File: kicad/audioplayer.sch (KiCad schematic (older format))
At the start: 29 parts, among them J1 Panel, J2 Charge_USB, J3 Speakers, J4 RFID, SW1 POWER, U1 PB-500, U2 ESP32-nodeMCU, U3 OLED, U4 GY-521, U5 VS1053/SD_breakout, U6 ULN2003, U7 HW-323

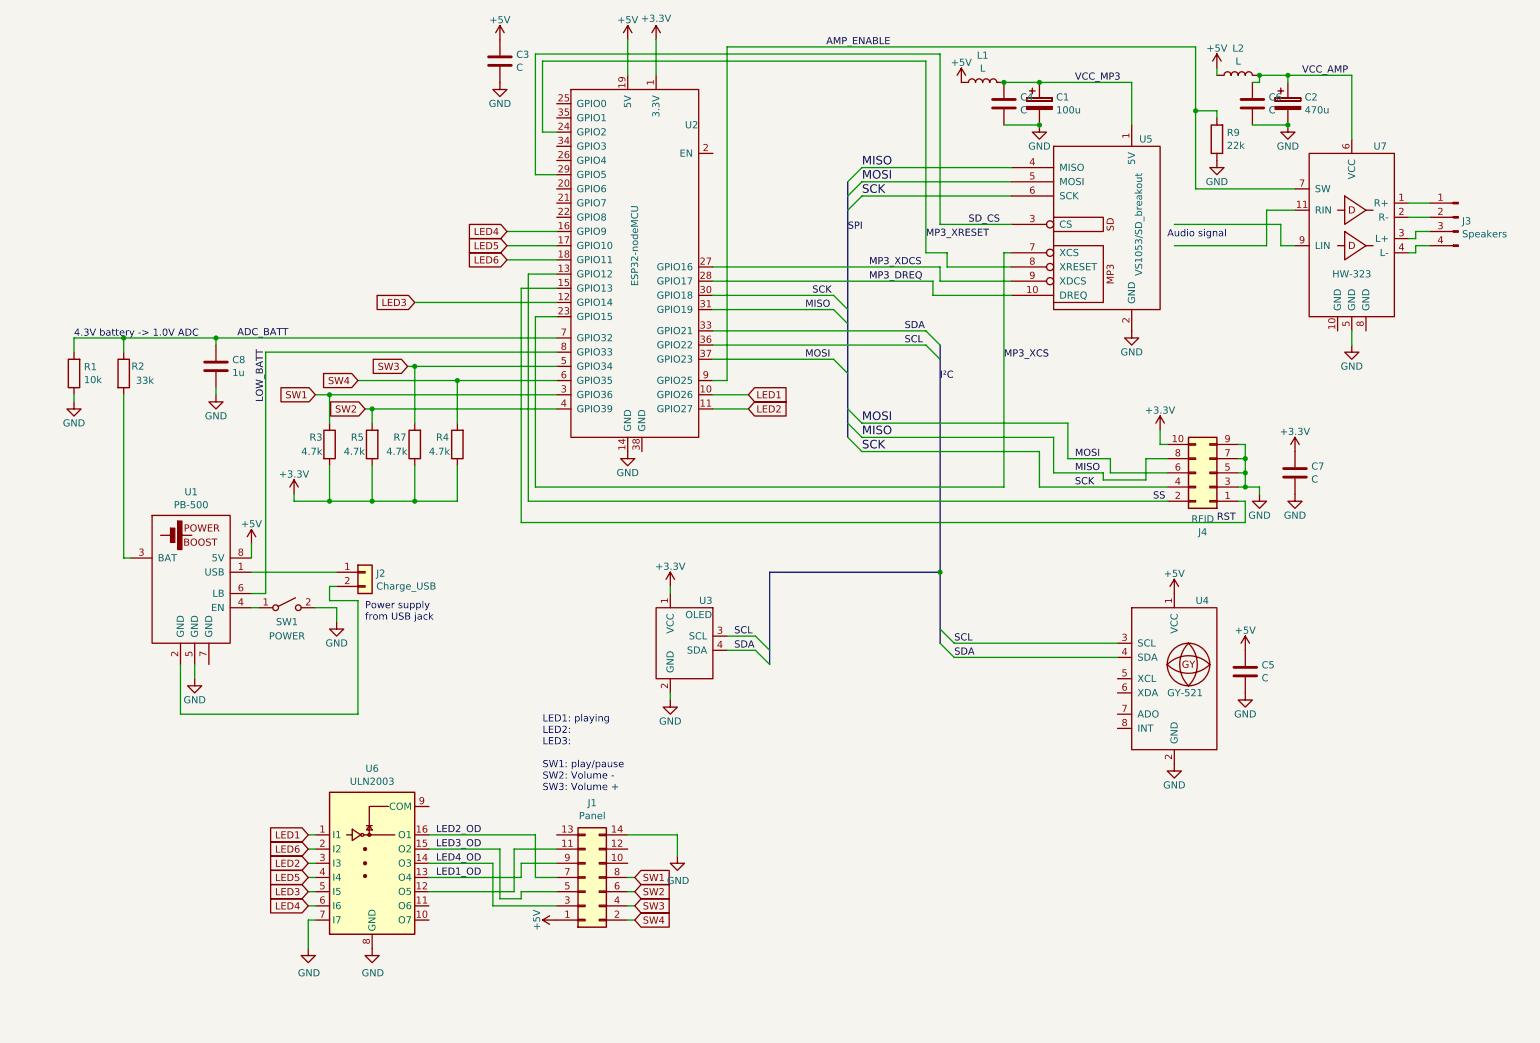
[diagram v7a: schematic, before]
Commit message: board revision 03
better ground handling, vastly reduced background noise
added reconstruction filter to vs1053 output
added possibillity to add headphone jack
use smd darlington array
add diode for battery low signal
add diode for charging connector (reverse polarity protection just in case)
use 10-pin panel connector and swapped connections for better PCB routing
swapped some GPIO-Pins for better PCB routing (i.e. RFID SS,SCK)
use restor ladder for button GPIOs
removed supply decoupling for SD/MP3 board
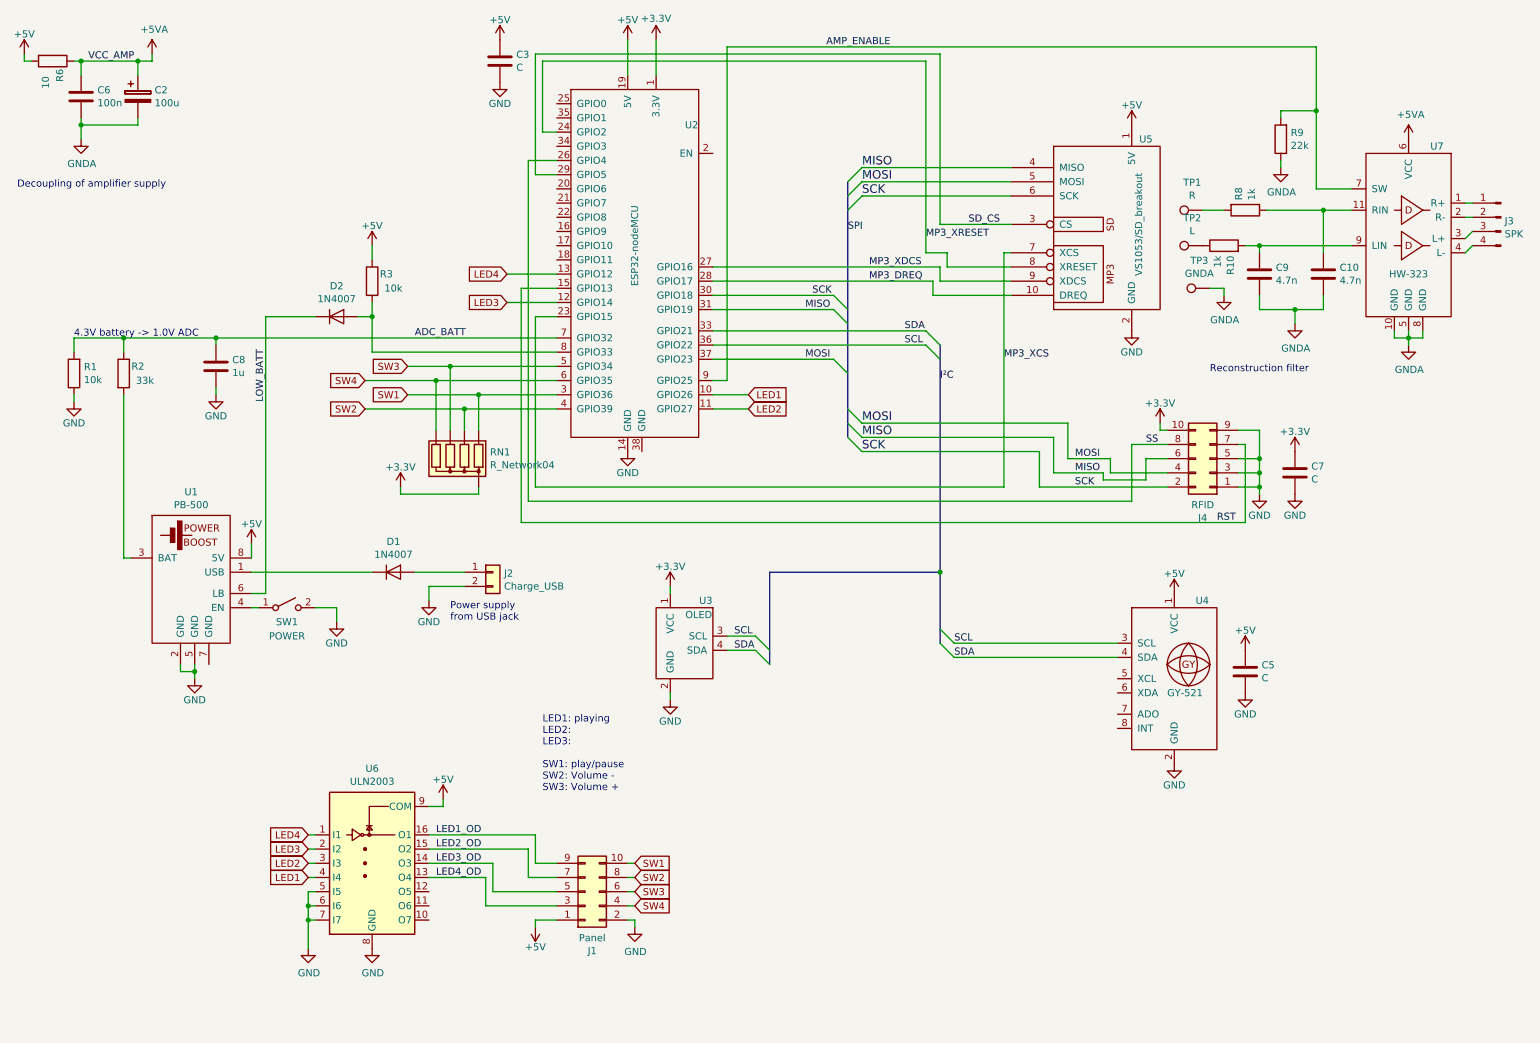
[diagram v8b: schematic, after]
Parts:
- removed C1: 100u, Capacitor_THT:CP_Radial_D10.0mm_P5.00mm, symbol Device:CP
- removed C4: C, Capacitor_THT:C_Disc_D5.1mm_W3.2mm_P5.00mm, symbol Device:C
- removed J1: Panel, Connector_PinHeader_2.54mm:PinHeader_2x07_P2.54mm_Vertical, symbol Connector_Generic:Conn_02x07_Odd_Even
- removed L1, L2: L, Inductor_THT:L_Axial_L6.6mm_D2.7mm_P10.16mm_Horizontal_Vishay_IM-2, symbol Device:L
- removed R4, R5, R7: 4.7k, Resistor_THT:R_Axial_DIN0204_L3.6mm_D1.6mm_P7.62mm_Horizontal, symbol Device:R
- added C10, C9: 4.7n, Capacitor_THT:C_Rect_L7.0mm_W2.5mm_P5.00mm, symbol Device:C
- added D1, D2: 1N4007, Diode_THT:D_DO-41_SOD81_P10.16mm_Horizontal, symbol Diode:1N4007
- added J1: Panel, Connector_PinHeader_2.54mm:PinHeader_2x05_P2.54mm_Vertical, symbol Connector_Generic:Conn_02x05_Odd_Even
- added R10, R8: 1k, Resistor_THT:R_Axial_DIN0204_L3.6mm_D1.6mm_P7.62mm_Horizontal, symbol Device:R
- added R6: 10, Resistor_THT:R_Axial_DIN0204_L3.6mm_D1.6mm_P7.62mm_Horizontal, symbol Device:R
- added RN1: R_Network04, Resistor_THT:R_Array_SIP5, symbol Device:R_Network04
- added TP1: R, Connector_PinHeader_2.54mm:PinHeader_1x01_P2.54mm_Vertical, symbol Connector:TestPoint
- added TP2: L, Connector_PinHeader_2.54mm:PinHeader_1x01_P2.54mm_Vertical, symbol Connector:TestPoint
- added TP3: GNDA, Connector_PinHeader_2.54mm:PinHeader_1x01_P2.54mm_Vertical, symbol Connector:TestPoint
- C2: value 470u -> 100u
- C6: value C -> 100n
- J3: value Speakers -> SPK
- R3: value 4.7k -> 10k
- U6: footprint Package_DIP:DIP-16_W7.62mm -> Package_SO:SOIC-16W_5.3x10.2mm_P1.27mm
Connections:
- net VCC_MP3 is gone; now on net +5V: U5.1 (5V)
- net +3V3: now also RN1.1 (common); no longer R3.2
- net +5V: now also R3.1, U6.9 (COM), J1.1 (Pin_1), R6.2
- net GND: now also J2.2 (Pin_2), J4.1 (Pin_1), U1.2 (GND), U6.5 (I5), U6.6 (I6), J1.2 (Pin_2); no longer C2.2, C6.2, J4.7 (Pin_7), R9.1, U7.5 (GND)
- net LED1: now also U6.4 (I4); no longer U6.1 (I1)
- net LED1_OD: now also U6.16 (O1), J1.9 (Pin_9); no longer U6.13 (O4)
- net LED2_OD: now also U6.15 (O2), J1.7 (Pin_7); no longer U6.16 (O1)
- net LED3: now also U6.2 (I2); no longer U6.5 (I5)
- net LED3_OD: now also U6.14 (O3), J1.5 (Pin_5); no longer U6.15 (O2)
- net LED4: now also U2.13 (GPIO12), U6.1 (I1); no longer U2.16 (GPIO9), U6.6 (I6)
- net LED4_OD: now also U6.13 (O4), J1.3 (Pin_3); no longer U6.14 (O3)
- net LOW_BATT: now also D2.1 (K); no longer U2.8 (GPIO33)
- net MISO: now also J4.6 (Pin_6); no longer J4.8 (Pin_8)
- net MOSI: now also J4.4 (Pin_4); no longer J4.6 (Pin_6)
- net RST: now also J4.7 (Pin_7); no longer J4.1 (Pin_1)
- net SCK: now also J4.2 (Pin_2); no longer J4.4 (Pin_4)
- net SS: now also J4.8 (Pin_8), U2.26 (GPIO4); no longer J4.2 (Pin_2), U2.13 (GPIO12)
- net SW1: now also J1.10 (Pin_10), RN1.2 (R1); no longer R3.1
- net SW2: now also J1.8 (Pin_8), RN1.3 (R2)
- net SW3: now also J1.6 (Pin_6), RN1.4 (R3)
- net SW4: now also J1.4 (Pin_4), RN1.5 (R4)
- net GNDA: now reaches U7.10 (GND)
- net GNDA: now also C2.2, C6.2, R9.1, U7.5 (GND), U7.8 (GND), C10.2, C9.2, TP3.1
- net at U7.11 (RIN): now also C10.1, R8.1
- net at U7.9 (LIN): now also C9.1, R10.2
- net at U1.1 (USB): now also D1.1 (K); no longer J2.1 (Pin_1)
- net LED5: no longer names the net of U2.17 (GPIO10)
- net LED5: no longer U6.4 (I4)
- net LED6: no longer names the net of U2.18 (GPIO11)
- net LED6: no longer U6.2 (I2)
- net VCC_AMP renamed +5VA
- net +5VA: now also R6.1
- new net: D2.2 (A), R3.2, U2.8 (GPIO33)
- new net: D1.2 (A), J2.1 (Pin_1)
- new net: R8.2, TP1.1
- new net: R10.1, TP2.1
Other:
- note added: "Decoupling of amplifier supply"
- note added: "Reconstruction filter"
- note removed: "Audio signal"
- moved on the sheet: C2, C6, J2, J3, J4, R9, U7
